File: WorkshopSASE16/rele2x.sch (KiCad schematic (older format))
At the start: 15 parts, among them J1 TB_1X3, J2 TB_1X3, K1 RELAY_C, K2 RELAY_C, Q1 2N3904, Q2 2N3904

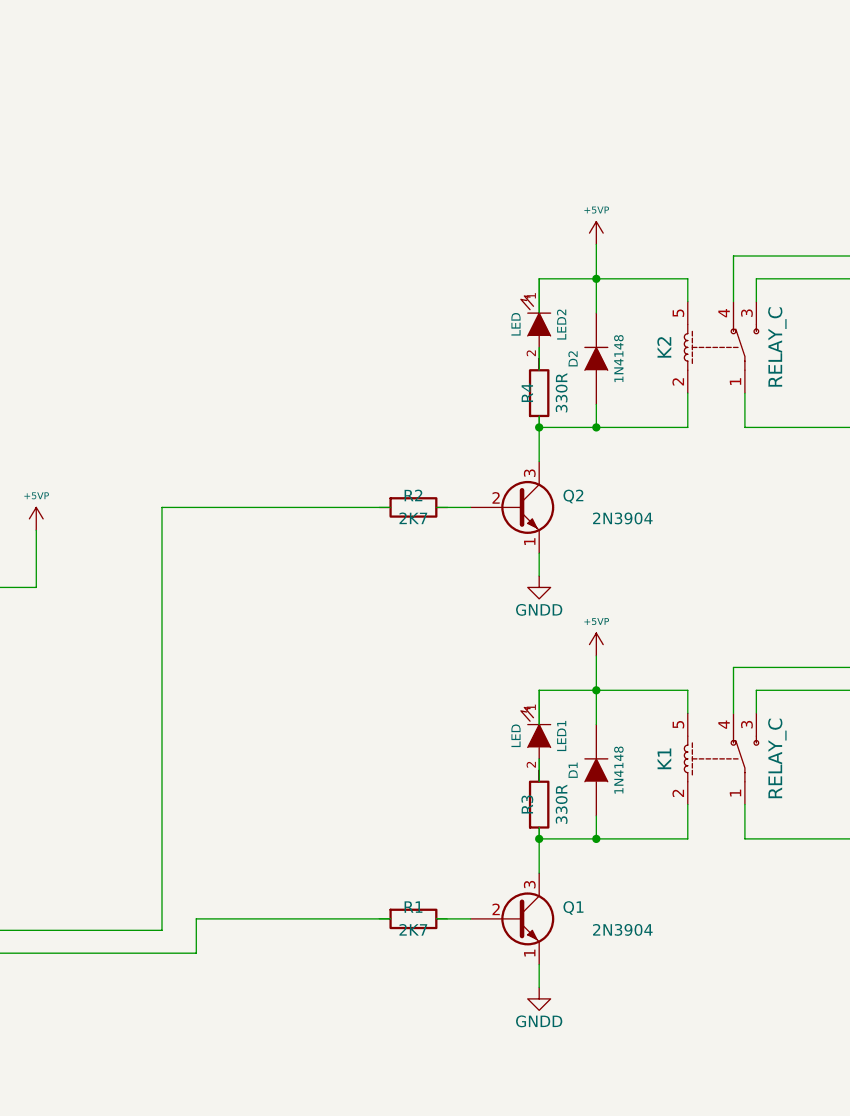
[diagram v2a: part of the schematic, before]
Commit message: Corrijo error de LED invertido por biblioteca device legqacy.
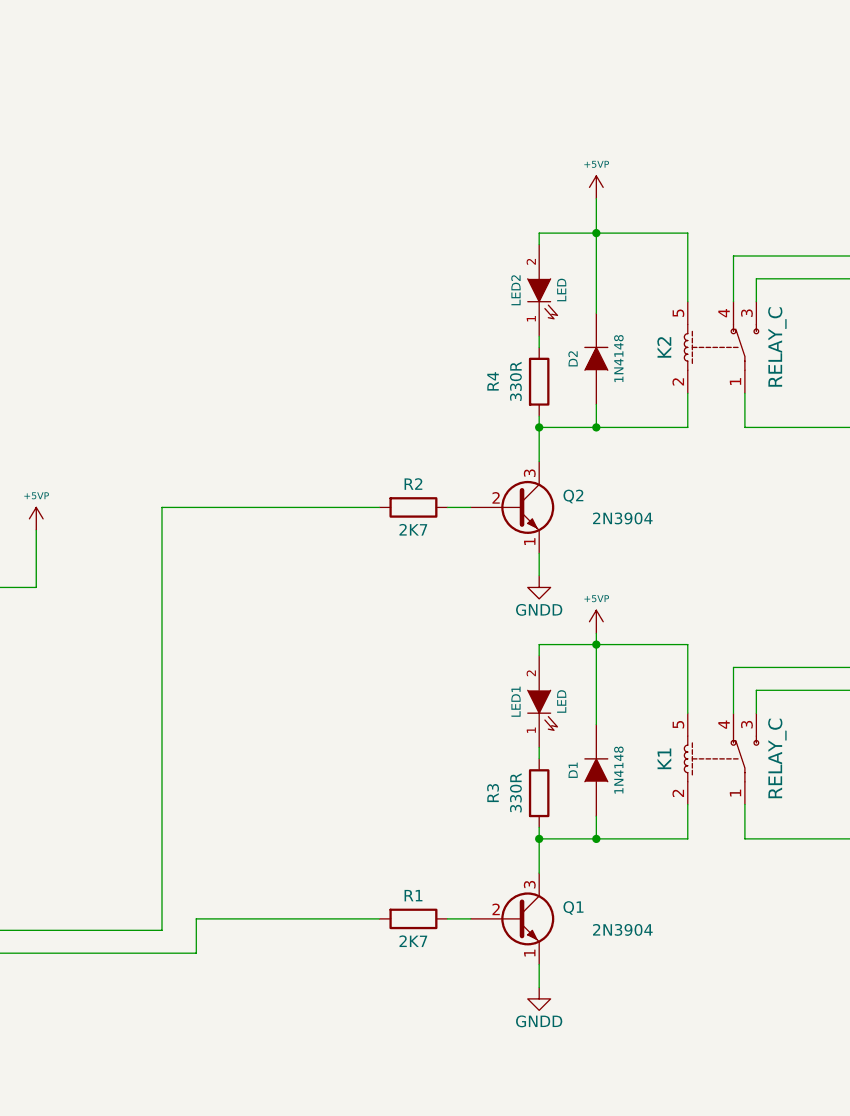
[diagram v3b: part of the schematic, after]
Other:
- moved on the sheet: LED1, LED2, R3, R4
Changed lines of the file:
@@
 EESchema Schematic File Version 2
-LIBS:power
+LIBS:device
 LIBS:rele2x-cache
 EELAYER 25 0
@@
 	5600 2250 5600 2350
 Connection ~ 5600 2350
-Wire Wire Line
-	5350 2100 5350 2000
 $Comp
 L +5VP #PWR010
 U 1 1 57A822EF
-P 5600 1550
-F 0 "#PWR010" H 5600 1640 20  0001 C CNN
-F 1 "+5VP" H 5600 1700 30  0000 C CNN
-F 2 "" H 5600 1550 60  0000 C CNN
-F 3 "" H 5600 1550 60  0000 C CNN
-	1    5600 1550
-	1    0    0    -1
-$EndComp
-Wire Wire Line
-	6000 1700 6000 1800
-Wire Wire Line
-	5350 1700 6000 1700
-Wire Wire Line
-	5350 1700 5350 1850
-Wire Wire Line
-	5600 1550 5600 1850
-Connection ~ 5600 1700
+P 5600 1350
+F 0 "#PWR010" H 5600 1440 20  0001 C CNN
+F 1 "+5VP" H 5600 1500 30  0000 C CNN
+F 2 "" H 5600 1350 60  0000 C CNN
+F 3 "" H 5600 1350 60  0000 C CNN
+	1    5600 1350
+	1    0    0    -1
+$EndComp
+Wire Wire Line
+	6000 1500 6000 1800
+Wire Wire Line
+	5350 1500 6000 1500
+Wire Wire Line
+	5600 1350 5600 1850
+Connection ~ 5600 1500
 Wire Wire Line
 	6950 2200 6800 2200
@@
 	5350 3000 5350 2900
 Wire Wire Line
-	5050 2700 4900 2700
-Wire Wire Line
 	1500 3050 1150 3050
 Wire Wire Line
@@
 L R R3
 U 1 1 57A976E4
-P 5350 4000
-F 0 "R3" V 5300 4000 50  0000 C CNN
-F 1 "330R" V 5450 4000 50  0000 C CNN
-F 2 "Resistors_ThroughHole:Resistor_Horizontal_RM10mm" H 5350 4000 60  0001 C CNN
-F 3 "" H 5350 4000 60  0000 C CNN
-F 4 "Stackpole" H 5350 4000 60  0001 C CNN "Manf"
-F 5 "CF14JT330R" H 5350 4000 60  0001 C CNN "Manf#"
-F 6 "CF14JT330RCT-ND" H 5350 4000 60  0001 C CNN "Digikey#"
-	1    5350 4000
+P 5350 3950
+F 0 "R3" V 5150 3950 50  0000 C CNN
+F 1 "330R" V 5250 3950 50  0000 C CNN
+F 2 "Resistors_ThroughHole:Resistor_Horizontal_RM10mm" H 5350 3950 60  0001 C CNN
+F 3 "" H 5350 3950 60  0000 C CNN
+F 4 "Stackpole" H 5350 3950 60  0001 C CNN "Manf"
+F 5 "CF14JT330R" H 5350 3950 60  0001 C CNN "Manf#"
+F 6 "CF14JT330RCT-ND" H 5350 3950 60  0001 C CNN "Digikey#"
+	1    5350 3950
 	1    0    0    -1
 $EndComp
@@
 L LED LED1
 U 1 1 57A976F0
-P 5350 3700
-F 0 "LED1" H 5350 3800 40  0000 C CNN
-F 1 "LED" H 5350 3600 40  0000 C CNN
-F 2 "LEDs:LED-3MM" H 5350 3700 60  0001 C CNN
-F 3 "" H 5350 3700 60  0000 C CNN
-F 4 "Marktech" H 5350 3700 60  0001 C CNN "Manf"
-F 5 "MT1403-RG-A" H 5350 3700 60  0001 C CNN "Manf#"
-F 6 "1125-1182-ND" H 5350 3700 60  0001 C CNN "Digikey#"
-	1    5350 3700
-	0    1    1    0
+P 5350 3550
+F 0 "LED1" H 5350 3650 40  0000 C CNN
+F 1 "LED" H 5350 3450 40  0000 C CNN
+F 2 "LEDs:LED-3MM" H 5350 3550 60  0001 C CNN
+F 3 "" H 5350 3550 60  0000 C CNN
+F 4 "Marktech" H 5350 3550 60  0001 C CNN "Manf"
+F 5 "MT1403-RG-A" H 5350 3550 60  0001 C CNN "Manf#"
+F 6 "1125-1182-ND" H 5350 3550 60  0001 C CNN "Digikey#"
+	1    5350 3550
+	0    -1   -1   0
 $EndComp
 $Comp
@@
 	5600 4050 5600 4150
 Connection ~ 5600 4150
-Wire Wire Line
-	5350 3900 5350 3800
 $Comp
 L +5VP #PWR013
 U 1 1 57A9770F
-P 5600 3350
-F 0 "#PWR013" H 5600 3440 20  0001 C CNN
-F 1 "+5VP" H 5600 3500 30  0000 C CNN
-F 2 "" H 5600 3350 60  0000 C CNN
-F 3 "" H 5600 3350 60  0000 C CNN
-	1    5600 3350
-	1    0    0    -1
-$EndComp
-Wire Wire Line
-	6000 3500 6000 3600
-Wire Wire Line
-	5350 3500 6000 3500
-Wire Wire Line
-	5350 3500 5350 3650
-Wire Wire Line
-	5600 3350 5600 3650
-Connection ~ 5600 3500
+P 5600 3250
+F 0 "#PWR013" H 5600 3340 20  0001 C CNN
+F 1 "+5VP" H 5600 3400 30  0000 C CNN
+F 2 "" H 5600 3250 60  0000 C CNN
+F 3 "" H 5600 3250 60  0000 C CNN
+	1    5600 3250
+	1    0    0    -1
+$EndComp
+Wire Wire Line
+	6000 3300 6000 3600
+Wire Wire Line
+	5600 3250 5600 3650
 Wire Wire Line
 	6950 4000 6800 4000
@@
 U 1 1 57A97726
 P 4800 4500
-F 0 "R1" V 4750 4500 50  0000 C CNN
-F 1 "2K7" V 4850 4500 50  0000 C CNN
+F 0 "R1" V 4700 4500 50  0000 C CNN
+F 1 "2K7" V 4900 4500 50  0000 C CNN
 F 2 "Resistors_ThroughHole:Resistor_Horizontal_RM10mm" H 4800 4500 60  0001 C CNN
 F 3 "" H 4800 4500 60  0000 C CNN
@@
 	1    0    0    -1
 $EndComp
-Wire Wire Line
-	5050 4500 4900 4500
 Text Notes 4150 7350 0    60   ~ 0
 ADVERTENCIA:\nLos componentes y sus valores se eligen\na los fines de realizar un ejercicio con KiCad.\nEn caso de querer construir el circuito, verificar \nprimero el circuito ya que este no esta verificado.
@@
 	2700 4650 3850 4650
 Wire Wire Line
-	4700 2700 3700 2700
-Wire Wire Line
 	3700 2700 3700 4550
 Wire Wire Line
@@
 Wire Wire Line
 	3850 4650 3850 4500
-Wire Wire Line
-	3850 4500 4700 4500
 Connection ~ 1300 4850
 Text Notes 7550 2050 0    79   ~ 16
@@
 L LED LED2
 U 1 1 57A98D62
-P 5350 1900
-F 0 "LED2" H 5350 2000 40  0000 C CNN
-F 1 "LED" H 5350 1800 40  0000 C CNN
-F 2 "LEDs:LED-3MM" H 5350 1900 60  0001 C CNN
-F 3 "" H 5350 1900 60  0000 C CNN
-F 4 "Marktech" H 5350 1900 60  0001 C CNN "Manf"
-F 5 "MT1403-RG-A" H 5350 1900 60  0001 C CNN "Manf#"
-F 6 "1125-1182-ND" H 5350 1900 60  0001 C CNN "Digikey#"
-	1    5350 1900
-	0    1    1    0
+P 5350 1750
+F 0 "LED2" H 5350 1850 40  0000 C CNN
+F 1 "LED" H 5350 1650 40  0000 C CNN
+F 2 "LEDs:LED-3MM" H 5350 1750 60  0001 C CNN
+F 3 "" H 5350 1750 60  0000 C CNN
+F 4 "Marktech" H 5350 1750 60  0001 C CNN "Manf"
+F 5 "MT1403-RG-A" H 5350 1750 60  0001 C CNN "Manf#"
+F 6 "1125-1182-ND" H 5350 1750 60  0001 C CNN "Digikey#"
+	1    5350 1750
+	0    -1   -1   0
 $EndComp
 $Comp
@@
 U 1 1 57A99A1E
 P 4800 2700
-F 0 "R2" V 4750 2700 50  0000 C CNN
-F 1 "2K7" V 4850 2700 50  0000 C CNN
+F 0 "R2" V 4700 2700 50  0000 C CNN
+F 1 "2K7" V 4900 2700 50  0000 C CNN
 F 2 "Resistors_ThroughHole:Resistor_Horizontal_RM10mm" H 4800 2700 60  0001 C CNN
 F 3 "" H 4800 2700 60  0000 C CNN
@@
 L R R4
 U 1 1 57A99D8A
-P 5350 2200
-F 0 "R4" V 5300 2200 50  0000 C CNN
-F 1 "330R" V 5450 2200 50  0000 C CNN
-F 2 "Resistors_ThroughHole:Resistor_Horizontal_RM10mm" H 5350 2200 60  0001 C CNN
-F 3 "" H 5350 2200 60  0000 C CNN
-F 4 "Stackpole" H 5350 2200 60  0001 C CNN "Manf"
-F 5 "CF14JT330R" H 5350 2200 60  0001 C CNN "Manf#"
-F 6 "CF14JT330RCT-ND" H 5350 2200 60  0001 C CNN "Digikey#"
-	1    5350 2200
-	1    0    0    -1
-$EndComp
+P 5350 2150
+F 0 "R4" V 5150 2150 50  0000 C CNN
+F 1 "330R" V 5250 2150 50  0000 C CNN
+F 2 "Resistors_ThroughHole:Resistor_Horizontal_RM10mm" H 5350 2150 60  0001 C CNN
+F 3 "" H 5350 2150 60  0000 C CNN
+F 4 "Stackpole" H 5350 2150 60  0001 C CNN "Manf"
+F 5 "CF14JT330R" H 5350 2150 60  0001 C CNN "Manf#"
+F 6 "CF14JT330RCT-ND" H 5350 2150 60  0001 C CNN "Digikey#"
+	1    5350 2150
+	1    0    0    -1
+$EndComp
+Wire Wire Line
+	5350 1550 5350 1500
+Wire Wire Line
+	5350 2000 5350 1950
+Wire Wire Line
+	5350 3800 5350 3750
+Wire Wire Line
+	5350 3350 5350 3300
+Wire Wire Line
+	5350 3300 6000 3300
+Connection ~ 5600 3300
+Wire Wire Line
+	5050 2700 4950 2700
+Wire Wire Line
+	4650 2700 3700 2700
+Wire Wire Line
+	5050 4500 4950 4500
+Wire Wire Line
+	3850 4500 4650 4500
 $EndSCHEMATC
